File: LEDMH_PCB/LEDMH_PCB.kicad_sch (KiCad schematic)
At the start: 2 parts, among them U1 ATtiny85-20S

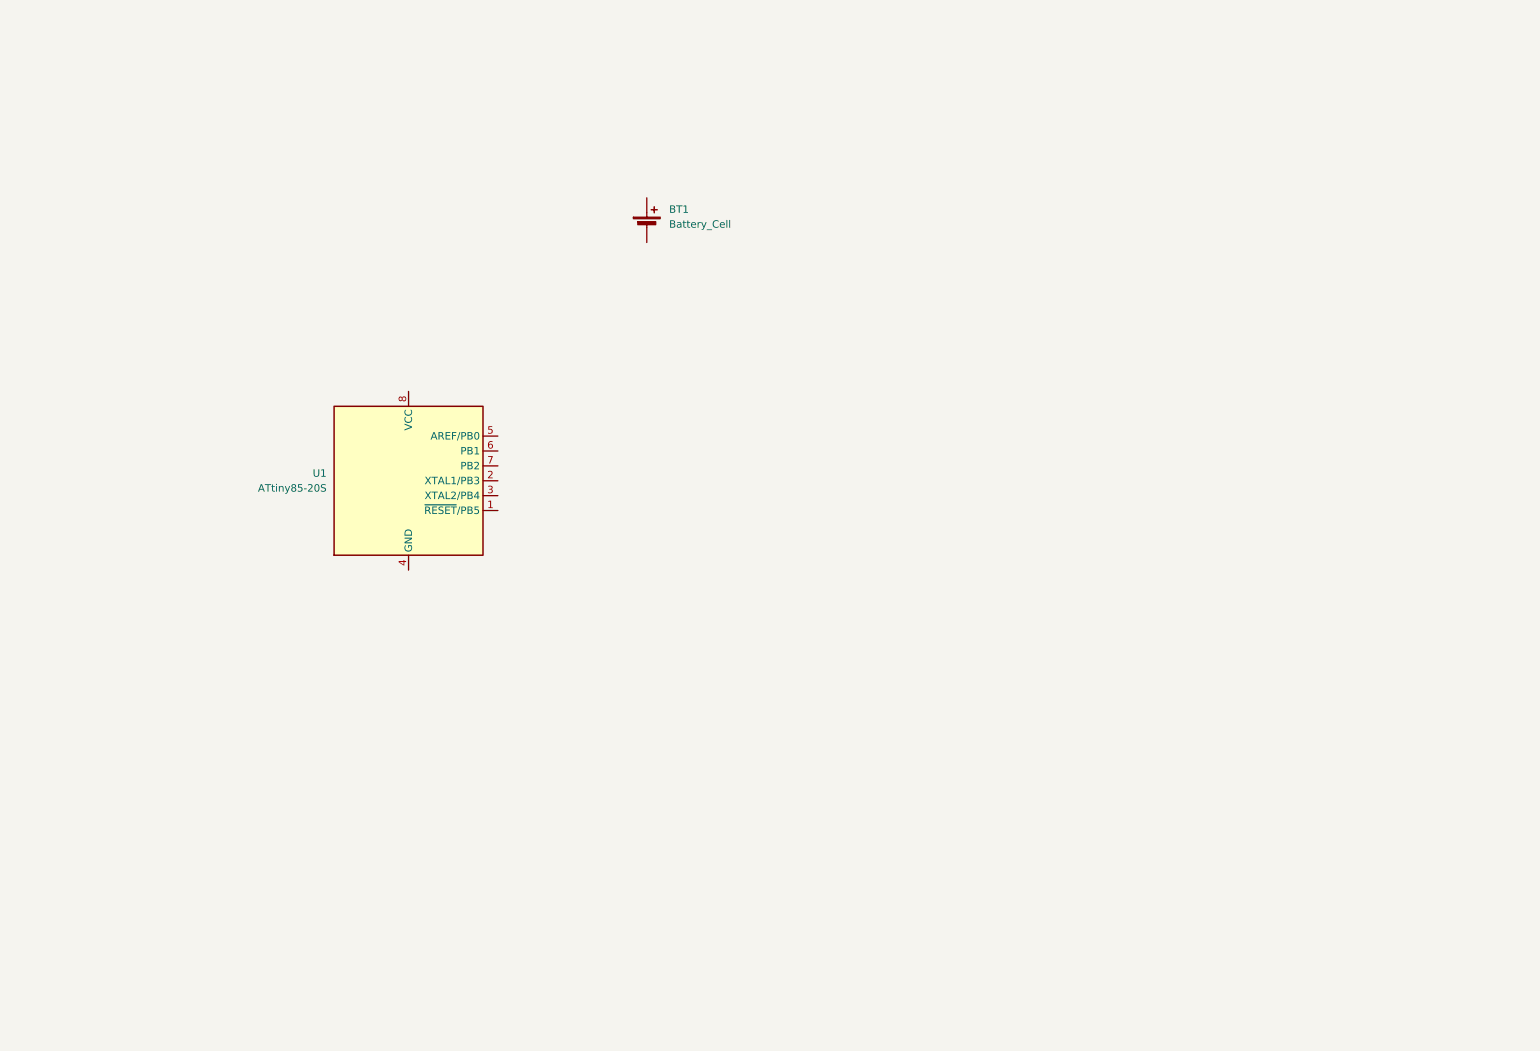
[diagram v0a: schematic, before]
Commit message: first revision of pcb
though the design will change because this isn't all on one board
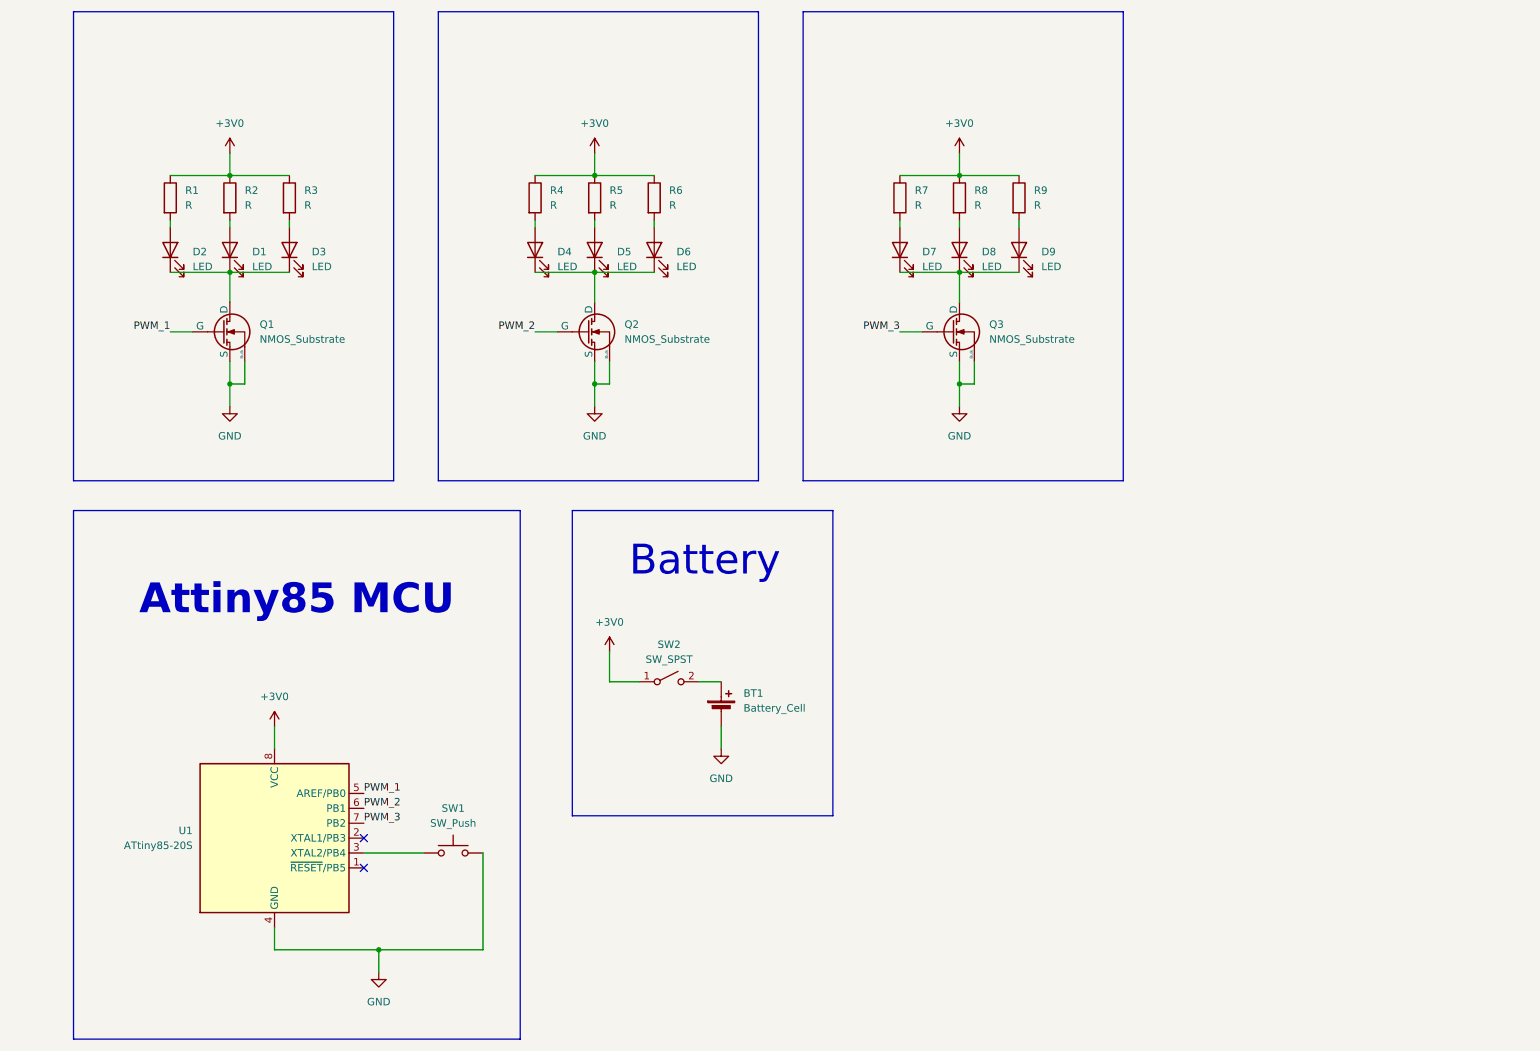
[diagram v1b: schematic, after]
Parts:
- added D1, D2, D3, D4, D5, D6, D7, D8, D9: LED, symbol Device:LED
- added Q1, Q2, Q3: NMOS_Substrate, symbol Simulation_SPICE:NMOS_Substrate
- added R1, R2, R3, R4, R5, R6, R7, R8, R9: R, symbol Device:R
- added SW1: SW_Push, symbol Switch:SW_Push
- added SW2: SW_SPST, symbol Switch:SW_SPST
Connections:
- net at U1.3 (XTAL2/PB4): now also SW1.1
- net GND: now reaches U1.4 (GND)
- net GND: now also BT1.2 (-), Q1.3 (S), Q1.4 (Bulk), Q2.3 (S), Q2.4 (Bulk), Q3.3 (S), Q3.4 (Bulk), SW1.2
- net PWM_1: now reaches U1.5 (AREF/PB0)
- net PWM_1: now also Q1.2 (G)
- net PWM_2: now reaches U1.6 (PB1)
- net PWM_2: now also Q2.2 (G)
- net PWM_3: now reaches U1.7 (PB2)
- net PWM_3: now also Q3.2 (G)
- net +3V0: now reaches U1.8 (VCC)
- net +3V0: now also R1.1, R2.1, R3.1, R4.1, R5.1, R6.1, R7.1, R8.1, R9.1, SW2.1 (A)
- net at BT1.1 (+): now also SW2.2 (B)
- new net: D4.1 (K), D5.1 (K), D6.1 (K), Q2.1 (D)
- new net: D3.2 (A), R3.2
- new net: D1.1 (K), D2.1 (K), D3.1 (K), Q1.1 (D)
- new net: D2.2 (A), R1.2
- new net: D4.2 (A), R4.2
- new net: D5.2 (A), R5.2
- new net: D9.2 (A), R9.2
- new net: D7.1 (K), D8.1 (K), D9.1 (K), Q3.1 (D)
- new net: D7.2 (A), R7.2
- new net: D6.2 (A), R6.2
- new net: D8.2 (A), R8.2
- new net: D1.2 (A), R2.2
- no-connect marks 0 -> 2
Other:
- note added: "Attiny85 MCU"
- note added: "Battery"
- moved on the sheet: BT1, U1

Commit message: added resistor value
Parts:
- R1, R2, R3, R4, R5, R6, R7, R8, R9: value R -> 140Ω
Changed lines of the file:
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@@
 			)
 		)
-		(property "Value" "R"
+		(property "Value" "140Ω"
 			(at 78.74 50.7999 0)
 			(effects
@@
 			)
 		)
-		(property "Value" "R"
+		(property "Value" "140Ω"
 			(at 130.81 50.7999 0)
 			(effects
@@
 			)
 		)
-		(property "Value" "R"
+		(property "Value" "140Ω"
 			(at 203.2 50.7999 0)
 			(effects
@@
 			)
 		)
-		(property "Value" "R"
+		(property "Value" "140Ω"
 			(at 140.97 50.7999 0)
 			(effects
@@
 			)
 		)
-		(property "Value" "R"
+		(property "Value" "140Ω"
 			(at 120.65 50.7999 0)
 			(effects
@@
 			)
 		)
-		(property "Value" "R"
+		(property "Value" "140Ω"
 			(at 193.04 50.7999 0)
 			(effects
@@
 			)
 		)
-		(property "Value" "R"
+		(property "Value" "140Ω"
 			(at 58.42 50.7999 0)
 			(effects
@@
 			)
 		)
-		(property "Value" "R"
+		(property "Value" "140Ω"
 			(at 68.58 50.7999 0)
 			(effects
@@
 			)
 		)
-		(property "Value" "R"
+		(property "Value" "140Ω"
 			(at 182.88 50.7999 0)
 			(effects

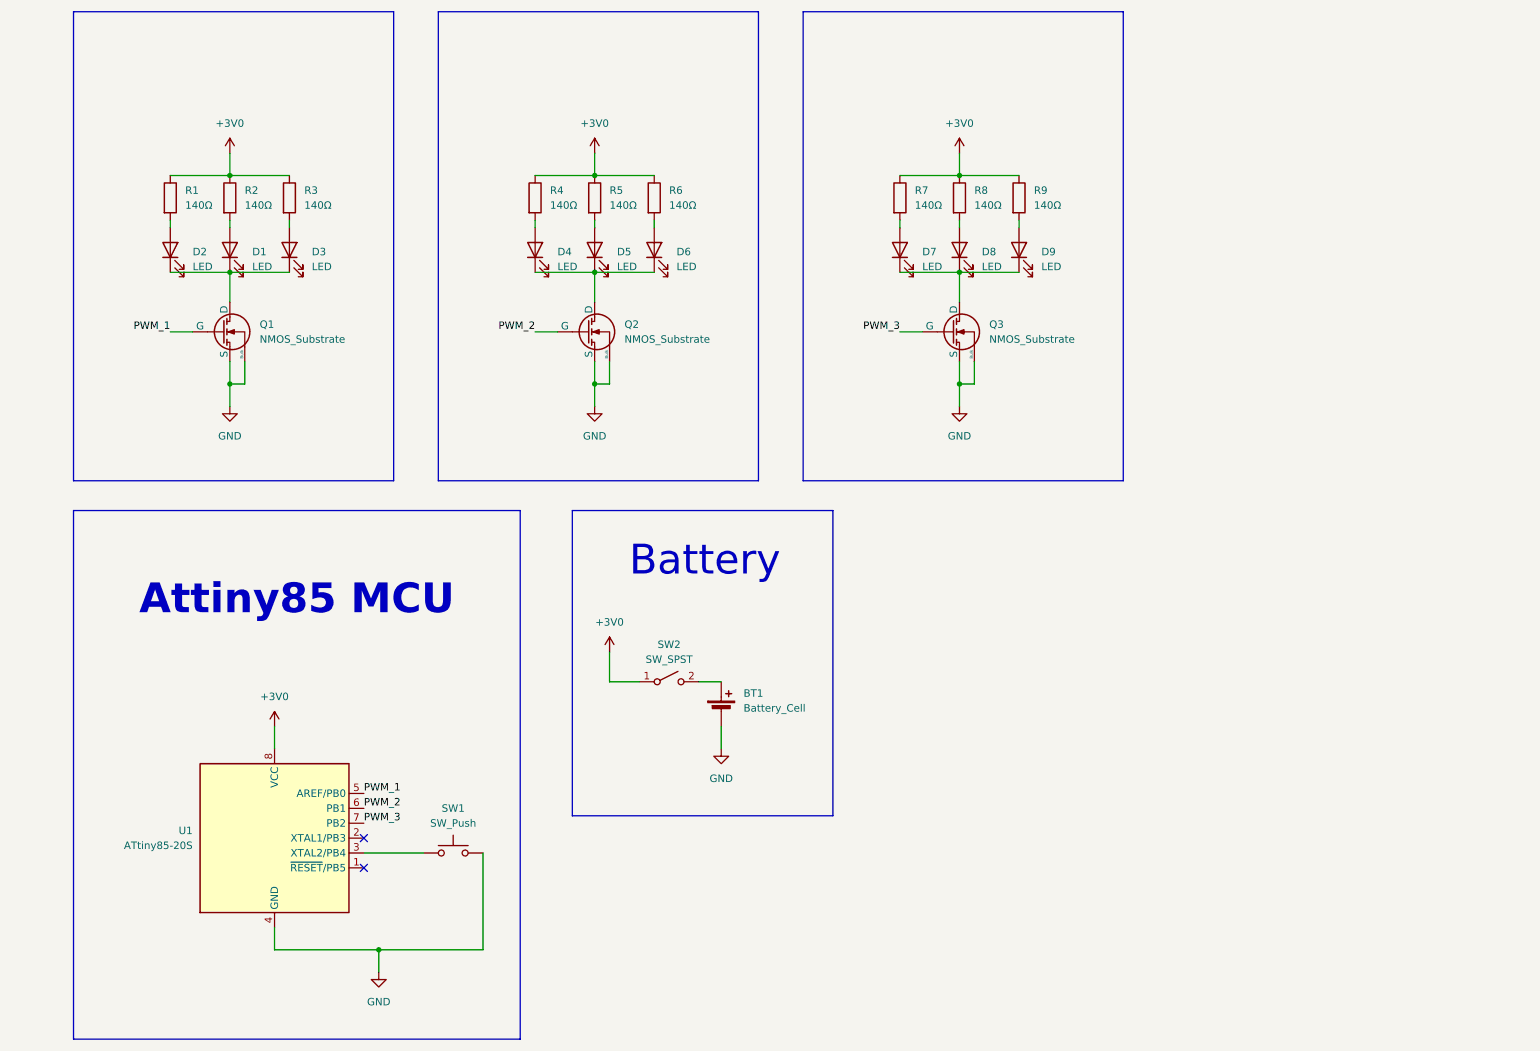
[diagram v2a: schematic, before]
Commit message: change R value, but that still needs to be changed, everything needs to be changed were gonna branch it for ver1.2 because im on a budget
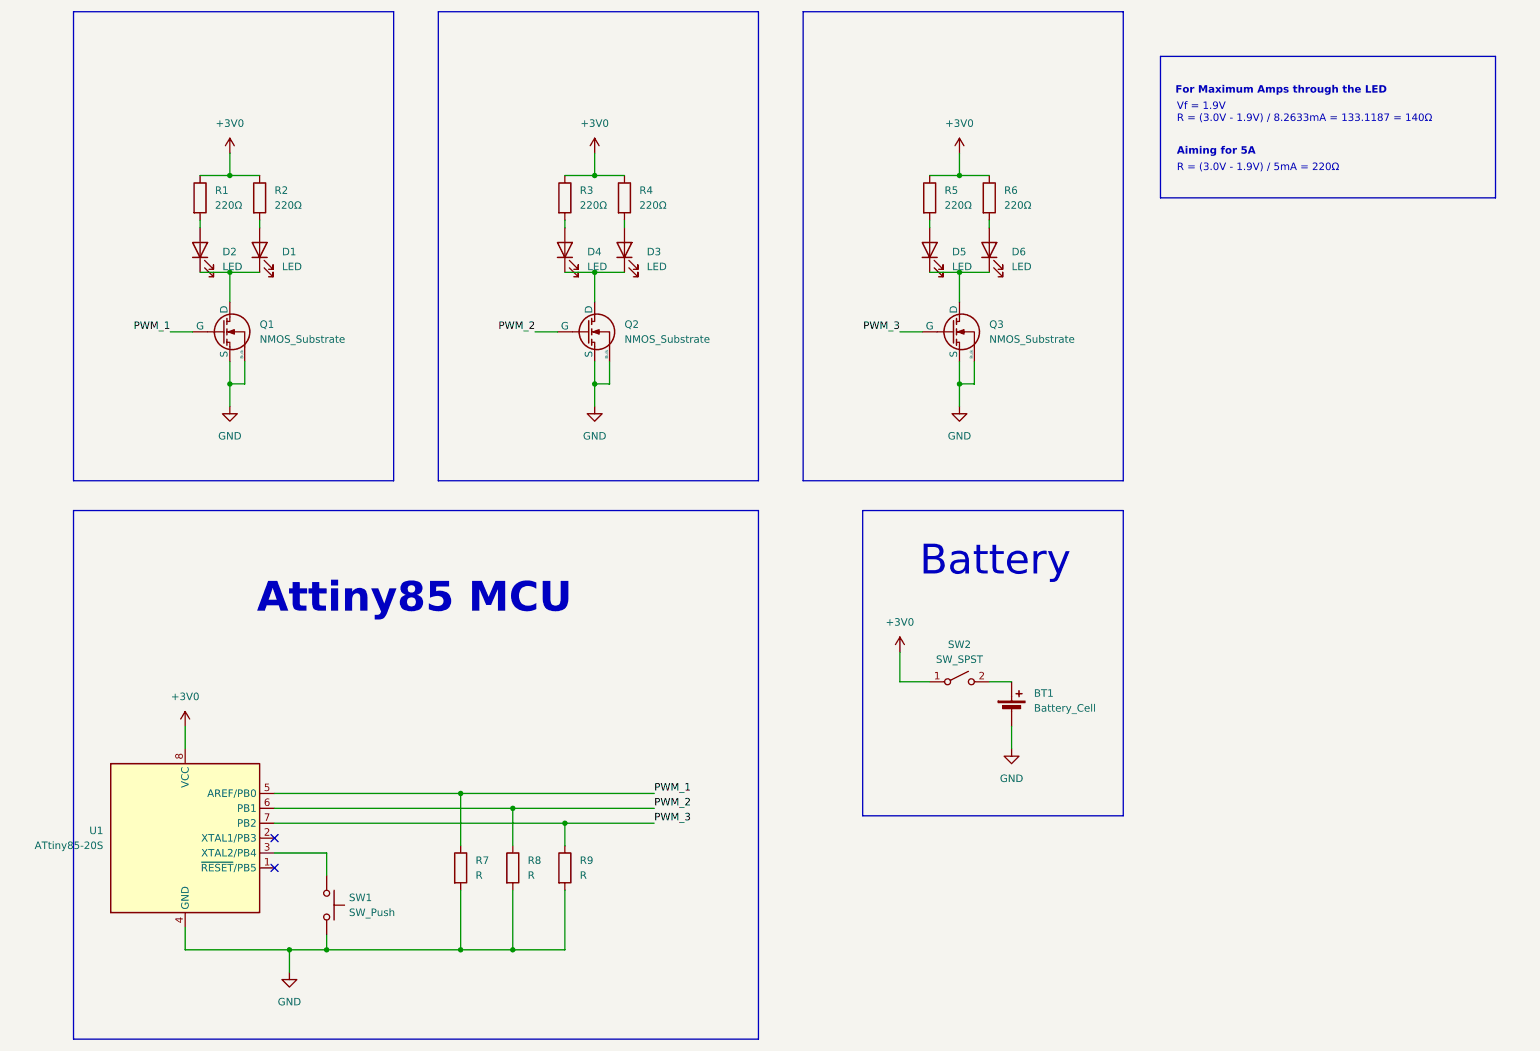
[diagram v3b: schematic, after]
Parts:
- removed D3, D6, D9: LED, symbol Device:LED
- removed R3, R6: 140Ω, symbol Device:R
- added R7, R8: R, symbol Device:R
- BT1: footprint (none) -> Battery:BatteryHolder_Keystone_3009_1x2450
- D1, D2, D4: footprint (none) -> LED_SMD:LED_Foshan-NTD3528_3.5x2.8mm
- D3: renamed from D5; footprint (none) -> LED_SMD:LED_Foshan-NTD3528_3.5x2.8mm
- D5: renamed from D7; footprint (none) -> LED_SMD:LED_Foshan-NTD3528_3.5x2.8mm
- D6: renamed from D8; footprint (none) -> LED_SMD:LED_Foshan-NTD3528_3.5x2.8mm
- R1, R2: value 140Ω -> 220Ω; footprint (none) -> Resistor_SMD:R_1206_3216Metric_Pad1.30x1.75mm_HandSolder
- R3: renamed from R4; value 140Ω -> 220Ω; footprint (none) -> Resistor_SMD:R_1206_3216Metric_Pad1.30x1.75mm_HandSolder
- R4: renamed from R5; value 140Ω -> 220Ω; footprint (none) -> Resistor_SMD:R_1206_3216Metric_Pad1.30x1.75mm_HandSolder
- R5: renamed from R7; value 140Ω -> 220Ω; footprint (none) -> Resistor_SMD:R_1206_3216Metric_Pad1.30x1.75mm_HandSolder
- R6: renamed from R8; value 140Ω -> 220Ω; footprint (none) -> Resistor_SMD:R_1206_3216Metric_Pad1.30x1.75mm_HandSolder
- R9: value 140Ω -> R
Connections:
- net +3V0: no longer R9.1
- net GND: now also R9.2, R7.2, R8.2
- net PWM_1: now also R7.1
- net PWM_2: now also R8.1
- net PWM_3: now also R9.1
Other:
- note added: "Aiming for 5A"
- note added: "For Maximum Amps through the LED"
- note added: "R = (3.0V - 1.9V) / 5mA = 220Ω"
- note added: "Vf = 1.9V R = (3.0V - 1.9V) / 8.2633mA = 133.1187 = 140Ω"
- moved on the sheet: BT1, D1, D2, D3, D4, D5, D6, R1, R2, R3, R4, R5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
